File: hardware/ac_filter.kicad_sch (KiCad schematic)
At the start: 3 parts

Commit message: done routing
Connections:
- net AC_L_FLT: no longer RV1.2
- net AC_L_IN: now also RV1.2
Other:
- moved on the sheet: RV1
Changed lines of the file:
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@@
 	(paper "A4")
+	(junction
+		(at 83.82 71.12)
+		(diameter 0)
+		(color 0 0 0 0)
+	)
 	(junction
 		(at 104.14 78.74)
@@
 	)
 	(junction
-		(at 111.76 78.74)
-		(diameter 0)
-		(color 0 0 0 0)
-	)
-	(junction
-		(at 111.76 71.12)
+		(at 83.82 78.74)
 		(diameter 0)
 		(color 0 0 0 0)
@@
 	(wire
 		(pts
-			(xy 104.14 71.12) (xy 111.76 71.12)
-		)
-		(stroke
-			(width 0)
-			(type default)
-		)
-	)
-	(wire
-		(pts
-			(xy 92.71 78.74) (xy 104.14 78.74)
-		)
-		(stroke
-			(width 0)
-			(type default)
-		)
-	)
-	(wire
-		(pts
-			(xy 111.76 78.74) (xy 123.19 78.74)
-		)
-		(stroke
-			(width 0)
-			(type default)
-		)
-	)
-	(wire
-		(pts
-			(xy 111.76 71.12) (xy 123.19 71.12)
+			(xy 83.82 78.74) (xy 104.14 78.74)
+		)
+		(stroke
+			(width 0)
+			(type default)
+		)
+	)
+	(wire
+		(pts
+			(xy 104.14 71.12) (xy 113.03 71.12)
+		)
+		(stroke
+			(width 0)
+			(type default)
+		)
+	)
+	(wire
+		(pts
+			(xy 81.28 78.74) (xy 83.82 78.74)
+		)
+		(stroke
+			(width 0)
+			(type default)
+		)
+	)
+	(wire
+		(pts
+			(xy 83.82 71.12) (xy 93.98 71.12)
 		)
 		(stroke
@@
 	(wire
 		(pts
-			(xy 92.71 71.12) (xy 93.98 71.12)
-		)
-		(stroke
-			(width 0)
-			(type default)
-		)
-	)
-	(wire
-		(pts
-			(xy 104.14 78.74) (xy 111.76 78.74)
+			(xy 81.28 71.12) (xy 83.82 71.12)
+		)
+		(stroke
+			(width 0)
+			(type default)
+		)
+	)
+	(wire
+		(pts
+			(xy 104.14 78.74) (xy 113.03 78.74)
 		)
 		(stroke
@@
 	(hierarchical_label "AC_N_IN"
 		(shape input)
-		(at 92.71 78.74 180)
+		(at 81.28 78.74 180)
 		(fields_autoplaced yes)
 		(effects
@@
 	(hierarchical_label "AC_L_IN"
 		(shape input)
-		(at 92.71 71.12 180)
+		(at 81.28 71.12 180)
 		(fields_autoplaced yes)
 		(effects
@@
 	(hierarchical_label "AC_L_FLT"
 		(shape input)
-		(at 123.19 71.12 0)
+		(at 113.03 71.12 0)
 		(fields_autoplaced yes)
 		(effects
@@
 	(hierarchical_label "AC_N_FLT"
 		(shape input)
-		(at 123.19 78.74 0)
+		(at 113.03 78.74 0)
 		(fields_autoplaced yes)
 		(effects
@@
 	(symbol
 		(lib_id "Device:Varistor")
-		(at 111.76 74.93 180)
+		(at 83.82 74.93 180)
 		(unit 1)
 		(exclude_from_sim no)
@@
 		(dnp no)
 		(property "Reference" "RV1"
-			(at 115.57 73.4067 0)
+			(at 87.63 73.4067 0)
 			(effects
 				(font
@@
 		)
 		(property "Value" "350V"
-			(at 115.57 75.9467 0)
+			(at 87.63 75.9467 0)
 			(effects
 				(font
@@
 		)
 		(property "Footprint" "Varistor:RV_Disc_D12mm_W4.2mm_P7.5mm"
-			(at 113.538 74.93 90)
+			(at 85.598 74.93 90)
 			(effects
 				(font
@@
 		)
 		(property "Datasheet" "~"
-			(at 111.76 74.93 0)
+			(at 83.82 74.93 0)
 			(effects
 				(font
@@
 		)
 		(property "Description" ""
-			(at 111.76 74.93 0)
-			(effects
-				(font
+			(at 83.82 74.93 0)
+			(effects
+				(font

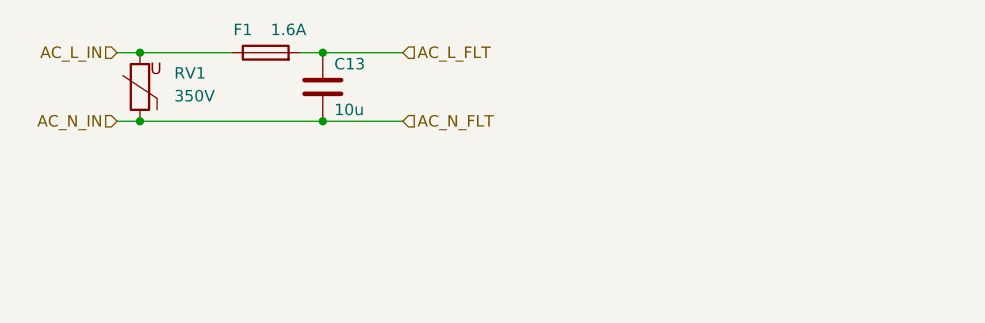
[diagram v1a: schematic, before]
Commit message: bugfix: triac output needs to confront L potential
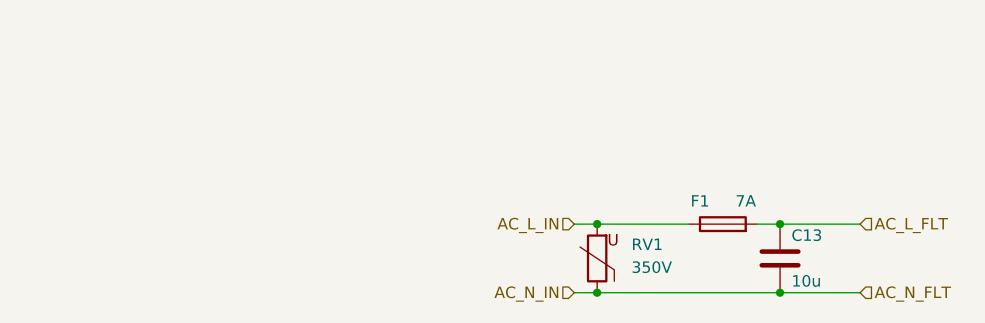
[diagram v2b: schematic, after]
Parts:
- F1: value 1.6A -> 7A
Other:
- moved on the sheet: C13, F1, RV1
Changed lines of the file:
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@@
 	(paper "A4")
 	(junction
-		(at 83.82 71.12)
+		(at 134.62 90.17)
 		(diameter 0)
 		(color 0 0 0 0)
 	)
 	(junction
-		(at 104.14 78.74)
+		(at 154.94 97.79)
 		(diameter 0)
 		(color 0 0 0 0)
 	)
 	(junction
-		(at 83.82 78.74)
+		(at 134.62 97.79)
 		(diameter 0)
 		(color 0 0 0 0)
 	)
 	(junction
-		(at 104.14 71.12)
+		(at 154.94 90.17)
 		(diameter 0)
 		(color 0 0 0 0)
@@
 	(wire
 		(pts
-			(xy 83.82 78.74) (xy 104.14 78.74)
-		)
-		(stroke
-			(width 0)
-			(type default)
-		)
-	)
-	(wire
-		(pts
-			(xy 104.14 71.12) (xy 113.03 71.12)
-		)
-		(stroke
-			(width 0)
-			(type default)
-		)
-	)
-	(wire
-		(pts
-			(xy 81.28 78.74) (xy 83.82 78.74)
-		)
-		(stroke
-			(width 0)
-			(type default)
-		)
-	)
-	(wire
-		(pts
-			(xy 83.82 71.12) (xy 93.98 71.12)
-		)
-		(stroke
-			(width 0)
-			(type default)
-		)
-	)
-	(wire
-		(pts
-			(xy 101.6 71.12) (xy 104.14 71.12)
-		)
-		(stroke
-			(width 0)
-			(type default)
-		)
-	)
-	(wire
-		(pts
-			(xy 81.28 71.12) (xy 83.82 71.12)
-		)
-		(stroke
-			(width 0)
-			(type default)
-		)
-	)
-	(wire
-		(pts
-			(xy 104.14 78.74) (xy 113.03 78.74)
+			(xy 134.62 97.79) (xy 154.94 97.79)
+		)
+		(stroke
+			(width 0)
+			(type default)
+		)
+	)
+	(wire
+		(pts
+			(xy 154.94 90.17) (xy 163.83 90.17)
+		)
+		(stroke
+			(width 0)
+			(type default)
+		)
+	)
+	(wire
+		(pts
+			(xy 132.08 97.79) (xy 134.62 97.79)
+		)
+		(stroke
+			(width 0)
+			(type default)
+		)
+	)
+	(wire
+		(pts
+			(xy 134.62 90.17) (xy 144.78 90.17)
+		)
+		(stroke
+			(width 0)
+			(type default)
+		)
+	)
+	(wire
+		(pts
+			(xy 152.4 90.17) (xy 154.94 90.17)
+		)
+		(stroke
+			(width 0)
+			(type default)
+		)
+	)
+	(wire
+		(pts
+			(xy 132.08 90.17) (xy 134.62 90.17)
+		)
+		(stroke
+			(width 0)
+			(type default)
+		)
+	)
+	(wire
+		(pts
+			(xy 154.94 97.79) (xy 163.83 97.79)
 		)
 		(stroke
@@
 	(hierarchical_label "AC_N_IN"
 		(shape input)
-		(at 81.28 78.74 180)
+		(at 132.08 97.79 180)
 		(fields_autoplaced yes)
 		(effects
@@
 	(hierarchical_label "AC_L_IN"
 		(shape input)
-		(at 81.28 71.12 180)
+		(at 132.08 90.17 180)
 		(fields_autoplaced yes)
 		(effects
@@
 	(hierarchical_label "AC_L_FLT"
 		(shape input)
-		(at 113.03 71.12 0)
+		(at 163.83 90.17 0)
 		(fields_autoplaced yes)
 		(effects
@@
 	(hierarchical_label "AC_N_FLT"
 		(shape input)
-		(at 113.03 78.74 0)
+		(at 163.83 97.79 0)
 		(fields_autoplaced yes)
 		(effects
@@
 	(symbol
 		(lib_id "Device:C")
-		(at 104.14 74.93 0)
+		(at 154.94 93.98 0)
 		(unit 1)
 		(exclude_from_sim no)
@@
 		(dnp no)
 		(property "Reference" "C13"
-			(at 105.41 72.39 0)
+			(at 156.21 91.44 0)
 			(effects
 				(font
@@
 		)
 		(property "Value" "10u"
-			(at 105.41 77.47 0)
+			(at 156.21 96.52 0)
 			(effects
 				(font
@@
 		)
 		(property "Footprint" "Capacitor_THT:C_Disc_D16.0mm_W5.0mm_P10.00mm"
-			(at 105.1052 78.74 0)
+			(at 155.9052 97.79 0)
 			(effects
 				(font
@@
 		)
 		(property "Datasheet" "~"
-			(at 104.14 74.93 0)
+			(at 154.94 93.98 0)
 			(effects
 				(font
@@
 		)
 		(property "Description" ""
-			(at 104.14 74.93 0)
+			(at 154.94 93.98 0)
 			(effects
 				(font
@@
 	(symbol
 		(lib_id "Device:Fuse")
-		(at 97.79 71.12 90)
+		(at 148.59 90.17 90)
 		(unit 1)
 		(exclude_from_sim no)
@@
 		(dnp no)
 		(property "Reference" "F1"
-			(at 95.25 68.58 90)
-			(effects
-				(font
-					(size 1.27 1.27)
-				)
-			)
-		)
-		(property "Value" "1.6A"
-			(at 100.33 68.58 90)
+			(at 146.05 87.63 90)
+			(effects
+				(font
+					(size 1.27 1.27)
+				)
+			)
+		)
+		(property "Value" "7A"
+			(at 151.13 87.63 90)
 			(effects
 				(font
@@
 		)
 		(property "Footprint" "Fuse:Fuse_Schurter_UMZ250"
-			(at 97.79 72.898 90)
+			(at 148.59 91.948 90)
 			(effects
 				(font
@@
 		)
 		(property "Datasheet" "~"
-			(at 97.79 71.12 0)
+			(at 148.59 90.17 0)
 			(effects
 				(font
@@
 		)
 		(property "Description" ""
-			(at 97.79 71.12 0)
+			(at 148.59 90.17 0)
 			(effects
 				(font
@@
 	(symbol
 		(lib_id "Device:Varistor")
-		(at 83.82 74.93 180)
+		(at 134.62 93.98 180)
 		(unit 1)
 		(exclude_from_sim no)
@@
 		(dnp no)
 		(property "Reference" "RV1"
-			(at 87.63 73.4067 0)
+			(at 138.43 92.4567 0)
 			(effects
 				(font
@@
 		)
 		(property "Value" "350V"
-			(at 87.63 75.9467 0)
+			(at 138.43 94.9967 0)
 			(effects
 				(font
@@
 		)
 		(property "Footprint" "Varistor:RV_Disc_D12mm_W4.2mm_P7.5mm"
-			(at 85.598 74.93 90)
+			(at 136.398 93.98 90)
 			(effects
 				(font
@@
 		)
 		(property "Datasheet" "~"
-			(at 83.82 74.93 0)
+			(at 134.62 93.98 0)
 			(effects
 				(font
@@
 		)
 		(property "Description" ""
-			(at 83.82 74.93 0)
-			(effects
-				(font
+			(at 134.62 93.98 0)
+			(effects
+				(font

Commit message: added some zones
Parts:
- F1: footprint Fuse:Fuse_Schurter_UMZ250 -> Fuse:Fuse_2512_6332Metric
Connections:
- net AC_L_FLT: no longer C13.1
- net AC_L_IN: now also C13.1
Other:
- moved on the sheet: C13, F1
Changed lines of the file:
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@@
-	)
-	(junction
-		(at 154.94 97.79)
-		(diameter 0)
-		(color 0 0 0 0)
 	)
 	(junction
@@
 	)
 	(junction
-		(at 154.94 90.17)
+		(at 148.59 90.17)
 		(diameter 0)
 		(color 0 0 0 0)
 	)
-	(wire
-		(pts
-			(xy 134.62 97.79) (xy 154.94 97.79)
-		)
-		(stroke
-			(width 0)
-			(type default)
-		)
-	)
-	(wire
-		(pts
-			(xy 154.94 90.17) (xy 163.83 90.17)
+	(junction
+		(at 148.59 97.79)
+		(diameter 0)
+		(color 0 0 0 0)
+	)
+	(wire
+		(pts
+			(xy 134.62 97.79) (xy 148.59 97.79)
+		)
+		(stroke
+			(width 0)
+			(type default)
+		)
+	)
+	(wire
+		(pts
+			(xy 148.59 97.79) (xy 163.83 97.79)
 		)
 		(stroke
@@
 	(wire
 		(pts
-			(xy 134.62 90.17) (xy 144.78 90.17)
-		)
-		(stroke
-			(width 0)
-			(type default)
-		)
-	)
-	(wire
-		(pts
-			(xy 152.4 90.17) (xy 154.94 90.17)
+			(xy 148.59 90.17) (xy 154.94 90.17)
+		)
+		(stroke
+			(width 0)
+			(type default)
+		)
+	)
+	(wire
+		(pts
+			(xy 134.62 90.17) (xy 148.59 90.17)
+		)
+		(stroke
+			(width 0)
+			(type default)
+		)
+	)
+	(wire
+		(pts
+			(xy 162.56 90.17) (xy 163.83 90.17)
 		)
 		(stroke
@@
 		(pts
 			(xy 132.08 90.17) (xy 134.62 90.17)
-		)
-		(stroke
-			(width 0)
-			(type default)
-		)
-	)
-	(wire
-		(pts
-			(xy 154.94 97.79) (xy 163.83 97.79)
 		)
 		(stroke
@@
 	(symbol
 		(lib_id "Device:C")
-		(at 154.94 93.98 0)
+		(at 148.59 93.98 0)
 		(unit 1)
 		(exclude_from_sim no)
@@
 		(dnp no)
 		(property "Reference" "C13"
-			(at 156.21 91.44 0)
+			(at 149.86 91.44 0)
 			(effects
 				(font
@@
 		)
 		(property "Value" "10u"
-			(at 156.21 96.52 0)
+			(at 149.86 96.52 0)
 			(effects
 				(font
@@
 		)
 		(property "Footprint" "Capacitor_THT:C_Disc_D16.0mm_W5.0mm_P10.00mm"
-			(at 155.9052 97.79 0)
+			(at 149.5552 97.79 0)
 			(effects
 				(font
@@
 		)
 		(property "Datasheet" "~"
-			(at 154.94 93.98 0)
+			(at 148.59 93.98 0)
 			(effects
 				(font
@@
 		)
 		(property "Description" ""
-			(at 154.94 93.98 0)
+			(at 148.59 93.98 0)
 			(effects
 				(font
@@
 	(symbol
 		(lib_id "Device:Fuse")
-		(at 148.59 90.17 90)
+		(at 158.75 90.17 90)
 		(unit 1)
 		(exclude_from_sim no)
@@
 		(dnp no)
 		(property "Reference" "F1"
-			(at 146.05 87.63 90)
+			(at 157.226 88.392 90)
 			(effects
 				(font
@@
 		)
 		(property "Value" "7A"
-			(at 151.13 87.63 90)
-			(effects
-				(font
-					(size 1.27 1.27)
-				)
-			)
-		)
-		(property "Footprint" "Fuse:Fuse_Schurter_UMZ250"
-			(at 148.59 91.948 90)
+			(at 160.274 88.392 90)
+			(effects
+				(font
+					(size 1.27 1.27)
+				)
+			)
+		)
+		(property "Footprint" "Fuse:Fuse_2512_6332Metric"
+			(at 158.75 91.948 90)
 			(effects
 				(font
@@
 		)
 		(property "Datasheet" "~"
-			(at 148.59 90.17 0)
+			(at 158.75 90.17 0)
 			(effects
 				(font
@@
 		)
 		(property "Description" ""
-			(at 148.59 90.17 0)
-			(effects
-				(font
+			(at 158.75 90.17 0)
+			(effects
+				(font

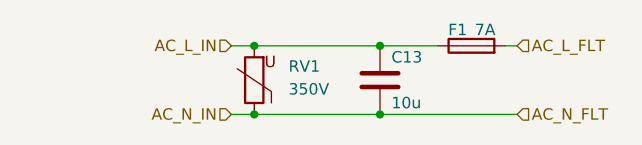
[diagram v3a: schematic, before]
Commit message: added some datasheets
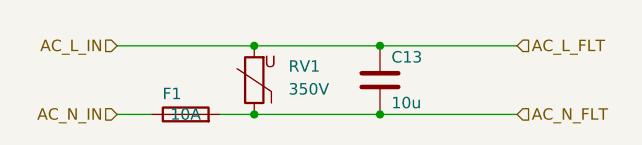
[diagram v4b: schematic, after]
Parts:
- F1: value 7A -> 10A; footprint Fuse:Fuse_2512_6332Metric -> Fuse:Fuseholder_Clip-5x20mm_Schurter_CQM_Inline_P20.60x5.00mm_D1.00mm_Horizontal
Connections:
- net AC_L_FLT: now also C13.1, RV1.2; no longer F1.2
- net AC_N_FLT: now also F1.2
- removed net AC_L_IN: C13.1, F1.1, RV1.2
- new net AC_N_IN: F1.1
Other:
- moved on the sheet: F1
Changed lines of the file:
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@@
 	(wire
 		(pts
-			(xy 132.08 97.79) (xy 134.62 97.79)
-		)
-		(stroke
-			(width 0)
-			(type default)
-		)
-	)
-	(wire
-		(pts
-			(xy 148.59 90.17) (xy 154.94 90.17)
+			(xy 148.59 90.17) (xy 163.83 90.17)
+		)
+		(stroke
+			(width 0)
+			(type default)
+		)
+	)
+	(wire
+		(pts
+			(xy 119.38 97.79) (xy 123.19 97.79)
 		)
 		(stroke
@@
 	(wire
 		(pts
-			(xy 162.56 90.17) (xy 163.83 90.17)
-		)
-		(stroke
-			(width 0)
-			(type default)
-		)
-	)
-	(wire
-		(pts
-			(xy 132.08 90.17) (xy 134.62 90.17)
+			(xy 119.38 90.17) (xy 134.62 90.17)
+		)
+		(stroke
+			(width 0)
+			(type default)
+		)
+	)
+	(wire
+		(pts
+			(xy 130.81 97.79) (xy 134.62 97.79)
 		)
 		(stroke
@@
 	(hierarchical_label "AC_N_IN"
 		(shape input)
-		(at 132.08 97.79 180)
+		(at 119.38 97.79 180)
 		(fields_autoplaced yes)
 		(effects
@@
 	(hierarchical_label "AC_L_IN"
 		(shape input)
-		(at 132.08 90.17 180)
+		(at 119.38 90.17 180)
 		(fields_autoplaced yes)
 		(effects
@@
 	(symbol
 		(lib_id "Device:Fuse")
-		(at 158.75 90.17 90)
+		(at 127 97.79 90)
 		(unit 1)
 		(exclude_from_sim no)
@@
 		(dnp no)
 		(property "Reference" "F1"
-			(at 157.226 88.392 90)
-			(effects
-				(font
-					(size 1.27 1.27)
-				)
-			)
-		)
-		(property "Value" "7A"
-			(at 160.274 88.392 90)
-			(effects
-				(font
-					(size 1.27 1.27)
-				)
-			)
-		)
-		(property "Footprint" "Fuse:Fuse_2512_6332Metric"
-			(at 158.75 91.948 90)
+			(at 125.476 95.504 90)
+			(effects
+				(font
+					(size 1.27 1.27)
+				)
+			)
+		)
+		(property "Value" "10A"
+			(at 127 97.79 90)
+			(effects
+				(font
+					(size 1.27 1.27)
+				)
+			)
+		)
+		(property "Footprint" "Fuse:Fuseholder_Clip-5x20mm_Schurter_CQM_Inline_P20.60x5.00mm_D1.00mm_Horizontal"
+			(at 127 99.568 90)
 			(effects
 				(font
@@
 		)
 		(property "Datasheet" "~"
-			(at 158.75 90.17 0)
+			(at 127 97.79 0)
 			(effects
 				(font
@@
 		)
 		(property "Description" ""
-			(at 158.75 90.17 0)
-			(effects
-				(font
+			(at 127 97.79 0)
+			(effects
+				(font

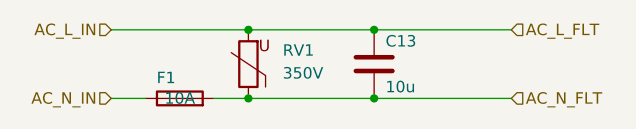
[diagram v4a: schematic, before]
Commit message: restructured copper planes
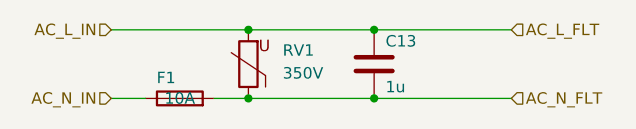
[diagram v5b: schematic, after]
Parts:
- C13: value 10u -> 1u; footprint Capacitor_THT:C_Disc_D16.0mm_W5.0mm_P10.00mm -> Capacitor_THT:C_Rect_L18.0mm_W8.0mm_P15.00mm_FKS3_FKP3
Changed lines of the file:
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@@
 			)
 		)
-		(property "Value" "10u"
+		(property "Value" "1u"
 			(at 149.86 96.52 0)
 			(effects
@@
 			)
 		)
-		(property "Footprint" "Capacitor_THT:C_Disc_D16.0mm_W5.0mm_P10.00mm"
+		(property "Footprint" "Capacitor_THT:C_Rect_L18.0mm_W8.0mm_P15.00mm_FKS3_FKP3"
 			(at 149.5552 97.79 0)
 			(effects
